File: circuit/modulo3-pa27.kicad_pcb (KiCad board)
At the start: 2 copper layers, 104 x 40 mm, 44 parts, among them SW1 bright, U1 OPA2134, U2 OPA2134, U3 TLE2426

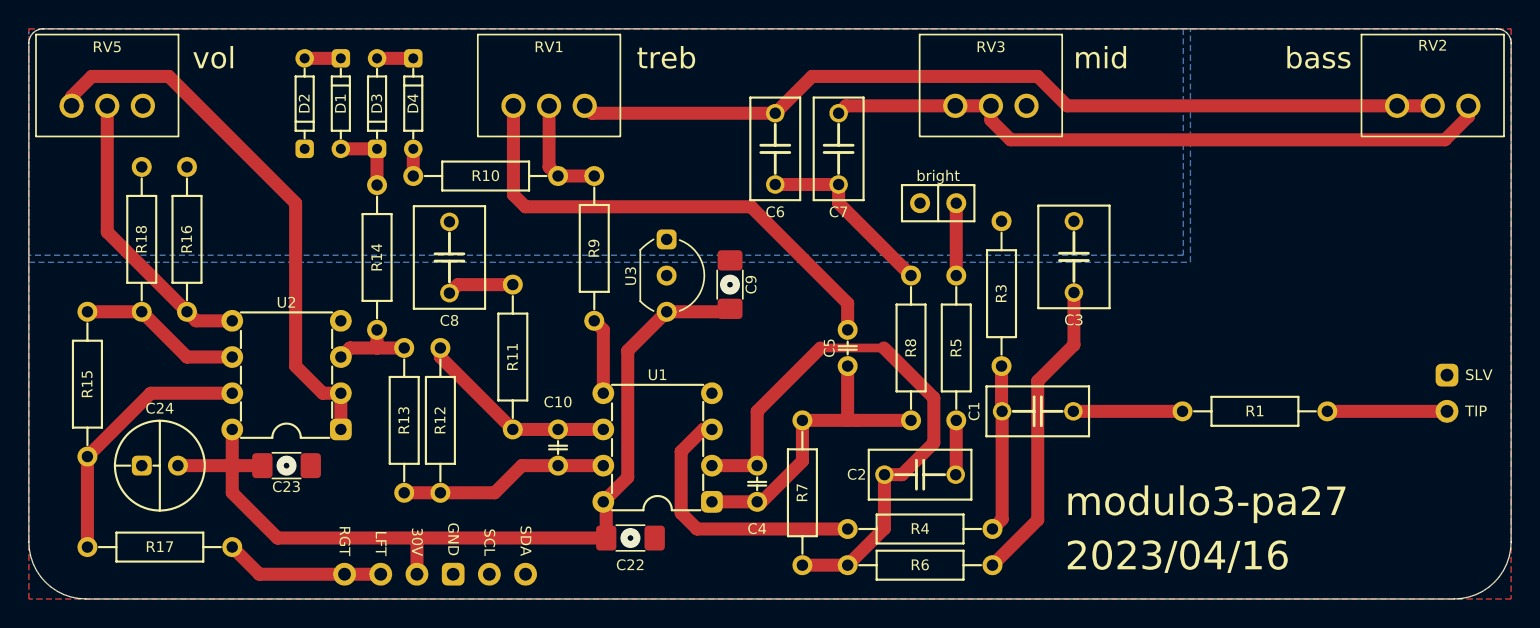
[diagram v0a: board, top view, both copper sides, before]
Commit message: fixed blunder in pa27; added stubs for some of the source files
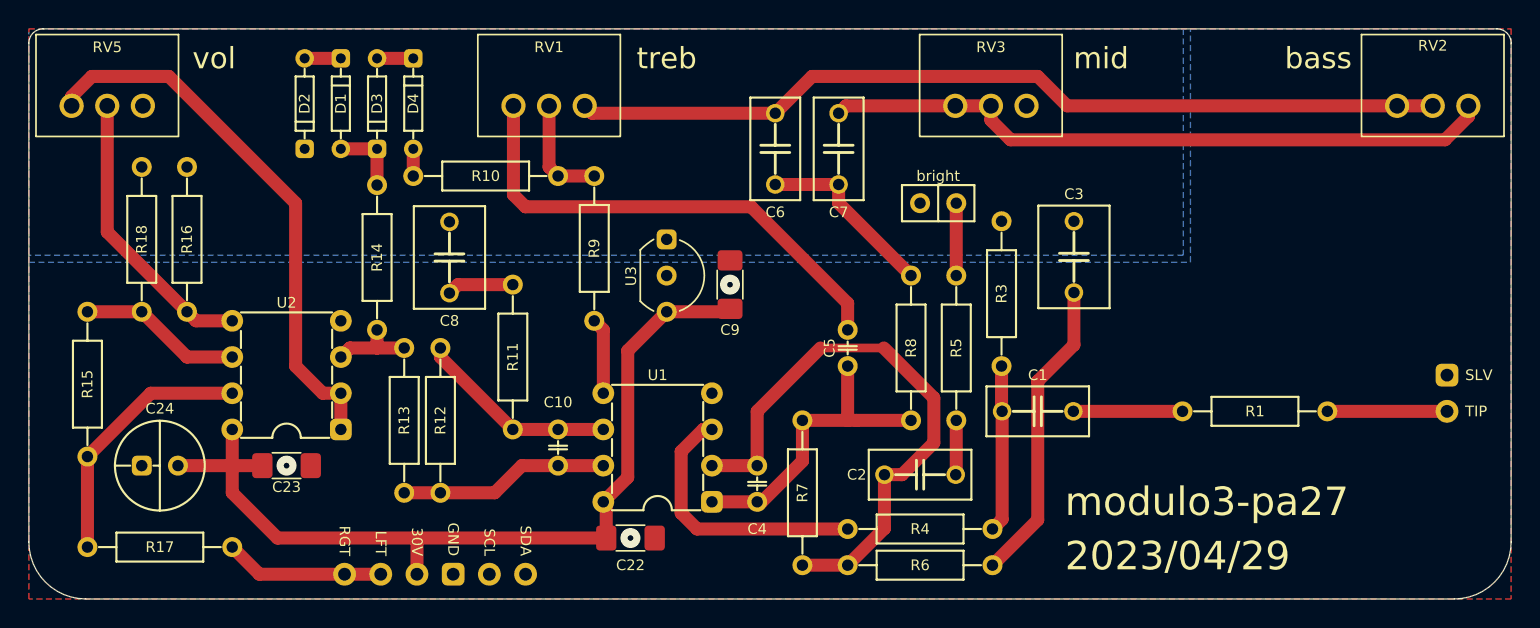
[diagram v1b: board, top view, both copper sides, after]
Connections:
- U5 pad 3: unconnected-(U5-GND-Pad3) -> GND
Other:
- board text added: "2023/04/29"
- board text removed: "2023/04/16"
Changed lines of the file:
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@@
   (net 30 "unconnected-(U5-SDA-Pad1)")
   (net 31 "unconnected-(U5-SCL-Pad2)")
-  (net 32 "unconnected-(U5-GND-Pad3)")
-  (net 33 "Net-(U4-TIP)")
+  (net 32 "Net-(U4-TIP)")
   (footprint "myAmp:C_FILM_L7.2mm_W5.0mm_P5.00mm" (layer "F.Cu")
     (at 123.825 66 -90)
@@
     (property "Sheetname" "")
     (attr through_hole)
-    (fp_text reference "C3" (at 4.445 0) (layer "F.SilkS")
+    (fp_text reference "C3" (at -4.405 0) (layer "F.SilkS")
         (effects (font (size 0.75 0.75) (thickness 0.15)))
     )
@@
     (property "Sheetname" "")
     (attr through_hole)
-    (fp_text reference "C1" (at 4.445 0 90) (layer "F.SilkS")
+    (fp_text reference "C1" (at 0 2.54 180) (layer "F.SilkS")
         (effects (font (size 0.75 0.75) (thickness 0.15)))
     )
@@
       (net 3 "Net-(C1-Pad1)") (pintype "passive"))
     (pad "2" thru_hole circle (at 5.08 0) (size 1.4 1.4) (drill 0.8) (layers "*.Cu" "*.Mask")
-      (net 33 "Net-(U4-TIP)") (pintype "passive"))
+      (net 32 "Net-(U4-TIP)") (pintype "passive"))
     (model "${KIPRJMOD}/myAmp.pretty/models/R_Axial_DIN0207_L6.3mm_D2.5mm_P10.16mm_Horizontal.step"
       (offset (xyz -5.08 0 0))
@@
     (property "Sheetname" "")
     (attr smd)
-    (fp_text reference "C9" (at 0 -1.5 -90) (layer "F.SilkS")
+    (fp_text reference "C9" (at 3.175 0) (layer "F.SilkS")
         (effects (font (size 0.75 0.75) (thickness 0.15)))
     )
@@
       (net 2 "GND") (pinfunction "SLEEVE") (pintype "input"))
     (pad "2" thru_hole circle (at 0 2.54 270) (size 1.6 1.6) (drill 0.9) (layers "*.Cu" "*.Mask")
-      (net 33 "Net-(U4-TIP)") (pinfunction "TIP") (pintype "input"))
+      (net 32 "Net-(U4-TIP)") (pinfunction "TIP") (pintype "input"))
     (model "${KIPRJMOD}/myAmp.pretty/models/PinHeader_1x02_P2.54mm_Vertical.wrl"
       (offset (xyz 0 0 0))
@@
       (net 31 "unconnected-(U5-SCL-Pad2)") (pinfunction "SCL") (pintype "input+no_connect"))
     (pad "3" thru_hole roundrect (at -1.27 0 180) (size 1.6 1.6) (drill 0.9) (layers "*.Cu" "*.Mask") (roundrect_rratio 0.25)
-      (net 32 "unconnected-(U5-GND-Pad3)") (pinfunction "GND") (pintype "input"))
+      (net 2 "GND") (pinfunction "GND") (pintype "input"))
     (pad "4" thru_hole circle (at 1.27 0 180) (size 1.6 1.6) (drill 0.9) (layers "*.Cu" "*.Mask")
       (net 1 "+28V") (pinfunction "30V") (pintype "input"))
@@
   (gr_arc (start 154.5 86) (mid 153.328427 88.828427) (end 150.5 90)
     (stroke (width 0.05) (type solid)) (layer "Edge.Cuts"))
-  (gr_text "2023/04/16" (at 123.19 86.995) (layer "F.SilkS")
+  (gr_text "2023/04/29" (at 123.19 86.995) (layer "F.SilkS")
     (effects (font (size 2 2) (thickness 0.3)) (justify left))
   )
@@
   (segment (start 149.86 57.785) (end 119.38 57.785) (width 0.9144) (layer "F.Cu") (net 29))
   (segment (start 107.835 55.4) (end 107.315 55.92) (width 0.9144) (layer "F.Cu") (net 29))
-  (segment (start 141.605 76.835) (end 150 76.835) (width 0.9144) (layer "F.Cu") (net 33))
+  (segment (start 141.605 76.835) (end 150 76.835) (width 0.9144) (layer "F.Cu") (net 32))
   (zone (net 2) (net_name "GND") (layer "F.Cu") (hatch edge 0.508)
     (connect_pads (clearance 0.254))
